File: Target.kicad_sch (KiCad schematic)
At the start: 63 parts, among them J10 PWR Header, J11 LP Extension Heder, J12 LP Header right, J13 PWR Header, J8 Jumper, J9 LP Header left, SW2 RESET, SW3 BOOT, U10 WS2812B-2020, U11 WS2812B-2020, U12 WS2812B-2020, U13 WS2812B-2020, U14 WS2812B-2020, U15 WS2812B-2020, U16 WS2812B-2020, U6 25Q64, U7 APS6404L-3SQR, U8 RP2350_80QFN, U9 WS2812B-2020, Y2 12MHz

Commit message: Renamed files.
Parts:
- J8: symbol rp2040-launchpad-PCB:Jumper -> rp2350b-launchpad-PCB:Jumper
- U10, U11, U12, U13, U14, U15, U16, U9: symbol rp2040-launchpad-PCB:WS2812B-2020 -> rp2350b-launchpad-PCB:WS2812B-2020
- U6: symbol rp2040-launchpad-PCB:25Q32 -> rp2350b-launchpad-PCB:25Q32
- U7: symbol rp2040-launchpad-PCB:APS6404L-3SQR -> rp2350b-launchpad-PCB:APS6404L-3SQR
- U8: symbol rp2040-launchpad-PCB:RP2350_80QFN -> rp2350b-launchpad-PCB:RP2350_80QFN
- USB2: symbol rp2040-launchpad-PCB:USB-C-Socket -> rp2350b-launchpad-PCB:USB-C-Socket
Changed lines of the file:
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@@
 	)
 	(symbol
-		(lib_id "rp2040-launchpad-PCB:25Q32")
+		(lib_id "rp2350b-launchpad-PCB:25Q32")
 		(at 46.99 153.67 0)
 		(mirror y)
@@
 	)
 	(symbol
-		(lib_id "rp2040-launchpad-PCB:WS2812B-2020")
+		(lib_id "rp2350b-launchpad-PCB:WS2812B-2020")
 		(at 165.1 139.7 0)
 		(unit 1)
@@
 	)
 	(symbol
-		(lib_id "rp2040-launchpad-PCB:WS2812B-2020")
+		(lib_id "rp2350b-launchpad-PCB:WS2812B-2020")
 		(at 180.34 139.7 0)
 		(unit 1)
@@
 	)
 	(symbol
-		(lib_id "rp2040-launchpad-PCB:WS2812B-2020")
+		(lib_id "rp2350b-launchpad-PCB:WS2812B-2020")
 		(at 195.58 139.7 0)
 		(unit 1)
@@
 	)
 	(symbol
-		(lib_id "rp2040-launchpad-PCB:WS2812B-2020")
+		(lib_id "rp2350b-launchpad-PCB:WS2812B-2020")
 		(at 210.82 139.7 0)
 		(unit 1)
@@
 	)
 	(symbol
-		(lib_id "rp2040-launchpad-PCB:WS2812B-2020")
+		(lib_id "rp2350b-launchpad-PCB:WS2812B-2020")
 		(at 226.06 139.7 0)
 		(unit 1)
@@
 	)
 	(symbol
-		(lib_id "rp2040-launchpad-PCB:WS2812B-2020")
+		(lib_id "rp2350b-launchpad-PCB:WS2812B-2020")
 		(at 241.3 139.7 0)
 		(unit 1)
@@
 	)
 	(symbol
-		(lib_id "rp2040-launchpad-PCB:WS2812B-2020")
+		(lib_id "rp2350b-launchpad-PCB:WS2812B-2020")
 		(at 256.54 139.7 0)
 		(unit 1)
@@
 	)
 	(symbol
-		(lib_id "rp2040-launchpad-PCB:WS2812B-2020")
+		(lib_id "rp2350b-launchpad-PCB:WS2812B-2020")
 		(at 271.78 139.7 0)
 		(unit 1)
@@
 		)
 		(instances
-			(project "rp2040-launchpad-PCB"
+			(project "rp2350b-launchpad-PCB"
 				(path "/60290668-847e-40fe-8544-1cbbc26023b6/00000000-0000-0000-0000-0000626cc112"
 					(reference "#PWR040")
@@
 		)
 		(instances
-			(project "rp2040-launchpad-PCB"
+			(project "rp2350b-launchpad-PCB"
 				(path "/60290668-847e-40fe-8544-1cbbc26023b6/00000000-0000-0000-0000-0000626cc112"
 					(reference "R29")
@@
 		)
 		(instances
-			(project "rp2040-launchpad-PCB"
+			(project "rp2350b-launchpad-PCB"
 				(path "/60290668-847e-40fe-8544-1cbbc26023b6/00000000-0000-0000-0000-0000626cc112"
 					(reference "#PWR046")
@@
 		)
 		(instances
-			(project "rp2040-launchpad-PCB"
+			(project "rp2350b-launchpad-PCB"
 				(path "/60290668-847e-40fe-8544-1cbbc26023b6/00000000-0000-0000-0000-0000626cc112"
 					(reference "R33")
@@
 		)
 		(instances
-			(project "rp2040-launchpad-PCB"
+			(project "rp2350b-launchpad-PCB"
 				(path "/60290668-847e-40fe-8544-1cbbc26023b6/00000000-0000-0000-0000-0000626cc112"
 					(reference "#PWR043")
@@
 		)
 		(instances
-			(project "rp2040-launchpad-PCB"
+			(project "rp2350b-launchpad-PCB"
 				(path "/60290668-847e-40fe-8544-1cbbc26023b6/00000000-0000-0000-0000-0000626cc112"
 					(reference "R32")
@@
 		)
 		(instances
-			(project "rp2040-launchpad-PCB"
+			(project "rp2350b-launchpad-PCB"
 				(path "/60290668-847e-40fe-8544-1cbbc26023b6/00000000-0000-0000-0000-0000626cc112"
 					(reference "R17")
@@
 		)
 		(instances
-			(project "rp2040-launchpad-PCB"
+			(project "rp2350b-launchpad-PCB"
 				(path "/60290668-847e-40fe-8544-1cbbc26023b6/00000000-0000-0000-0000-0000626cc112"
 					(reference "L2")
@@
 		)
 		(instances
-			(project "rp2040-launchpad-PCB"
+			(project "rp2350b-launchpad-PCB"
 				(path "/60290668-847e-40fe-8544-1cbbc26023b6/00000000-0000-0000-0000-0000626cc112"
 					(reference "C24")
@@
 		)
 		(instances
-			(project "rp2040-launchpad-PCB"
+			(project "rp2350b-launchpad-PCB"
 				(path "/60290668-847e-40fe-8544-1cbbc26023b6/00000000-0000-0000-0000-0000626cc112"
 					(reference "#PWR034")
@@
 		)
 		(instances
-			(project "rp2040-launchpad-PCB"
+			(project "rp2350b-launchpad-PCB"
 				(path "/60290668-847e-40fe-8544-1cbbc26023b6/00000000-0000-0000-0000-0000626cc112"
 					(reference "C26")
@@
 		)
 		(instances
-			(project "rp2040-launchpad-PCB"
+			(project "rp2350b-launchpad-PCB"
 				(path "/60290668-847e-40fe-8544-1cbbc26023b6/00000000-0000-0000-0000-0000626cc112"
 					(reference "#PWR035")
@@
 		)
 		(instances
-			(project "rp2040-launchpad-PCB"
+			(project "rp2350b-launchpad-PCB"
 				(path "/60290668-847e-40fe-8544-1cbbc26023b6/00000000-0000-0000-0000-0000626cc112"
 					(reference "R30")
@@
 		)
 		(instances
-			(project "rp2040-launchpad-PCB"
+			(project "rp2350b-launchpad-PCB"
 				(path "/60290668-847e-40fe-8544-1cbbc26023b6/00000000-0000-0000-0000-0000626cc112"
 					(reference "C29")
@@
 		)
 		(instances
-			(project "rp2040-launchpad-PCB"
+			(project "rp2350b-launchpad-PCB"
 				(path "/60290668-847e-40fe-8544-1cbbc26023b6/00000000-0000-0000-0000-0000626cc112"
 					(reference "#PWR038")
@@
 		)
 		(instances
-			(project "rp2040-launchpad-PCB"
+			(project "rp2350b-launchpad-PCB"
 				(path "/60290668-847e-40fe-8544-1cbbc26023b6/00000000-0000-0000-0000-0000626cc112"
 					(reference "R20")
@@
 		)
 		(instances
-			(project "rp2040-launchpad-PCB"
+			(project "rp2350b-launchpad-PCB"
 				(path "/60290668-847e-40fe-8544-1cbbc26023b6/00000000-0000-0000-0000-0000626cc112"
 					(reference "#PWR026")
@@
 		)
 		(instances
-			(project "rp2040-launchpad-PCB"
+			(project "rp2350b-launchpad-PCB"
 				(path "/60290668-847e-40fe-8544-1cbbc26023b6/00000000-0000-0000-0000-0000626cc112"
 					(reference "C30")
@@
 		)
 		(instances
-			(project "rp2040-launchpad-PCB"
+			(project "rp2350b-launchpad-PCB"
 				(path "/60290668-847e-40fe-8544-1cbbc26023b6/00000000-0000-0000-0000-0000626cc112"
 					(reference "S2")
@@
 		)
 		(instances
-			(project "rp2040-launchpad-PCB"
+			(project "rp2350b-launchpad-PCB"
 				(path "/60290668-847e-40fe-8544-1cbbc26023b6/00000000-0000-0000-0000-0000626cc112"
 					(reference "R18")
@@
 		)
 		(instances
-			(project "rp2040-launchpad-PCB"
+			(project "rp2350b-launchpad-PCB"
 				(path "/60290668-847e-40fe-8544-1cbbc26023b6/00000000-0000-0000-0000-0000626cc112"
 					(reference "#PWR031")
@@
 		)
 		(instances
-			(project "rp2040-launchpad-PCB"
+			(project "rp2350b-launchpad-PCB"
 				(path "/60290668-847e-40fe-8544-1cbbc26023b6/00000000-0000-0000-0000-0000626cc112"
 					(reference "#PWR033")
@@
 		)
 		(instances
-			(project "rp2040-launchpad-PCB"
+			(project "rp2350b-launchpad-PCB"
 				(path "/60290668-847e-40fe-8544-1cbbc26023b6/00000000-0000-0000-0000-0000626cc112"
 					(reference "#PWR030")
@@
 	)
 	(symbol
-		(lib_id "rp2040-launchpad-PCB:RP2350_80QFN")
+		(lib_id "rp2350b-launchpad-PCB:RP2350_80QFN")
 		(at 97.79 99.06 0)
 		(unit 1)
@@
 		)
 		(instances
-			(project "rp2040-launchpad-PCB"
+			(project "rp2350b-launchpad-PCB"
 				(path "/60290668-847e-40fe-8544-1cbbc26023b6/00000000-0000-0000-0000-0000626cc112"
 					(reference "C25")
@@
 		)
 		(instances
-			(project "rp2040-launchpad-PCB"
+			(project "rp2350b-launchpad-PCB"
 				(path "/60290668-847e-40fe-8544-1cbbc26023b6/00000000-0000-0000-0000-0000626cc112"
 					(reference "#PWR041")
@@
 		)
 		(instances
-			(project "rp2040-launchpad-PCB"
+			(project "rp2350b-launchpad-PCB"
 				(path "/60290668-847e-40fe-8544-1cbbc26023b6/00000000-0000-0000-0000-0000626cc112"
 					(reference "C31")
@@
 		)
 		(instances
-			(project "rp2040-launchpad-PCB"
+			(project "rp2350b-launchpad-PCB"
 				(path "/60290668-847e-40fe-8544-1cbbc26023b6/00000000-0000-0000-0000-0000626cc112"
 					(reference "R28")
@@
 	)
 	(symbol
-		(lib_id "rp2040-launchpad-PCB:APS6404L-3SQR")
+		(lib_id "rp2350b-launchpad-PCB:APS6404L-3SQR")
 		(at 48.26 182.88 0)
 		(unit 1)
@@
 		)
 		(instances
-			(project "rp2040-launchpad-PCB"
+			(project "rp2350b-launchpad-PCB"
 				(path "/60290668-847e-40fe-8544-1cbbc26023b6/00000000-0000-0000-0000-0000626cc112"
 					(reference "R26")
@@
 		)
 		(instances
-			(project "rp2040-launchpad-PCB"
+			(project "rp2350b-launchpad-PCB"
 				(path "/60290668-847e-40fe-8544-1cbbc26023b6/00000000-0000-0000-0000-0000626cc112"
 					(reference "#PWR042")
@@
 	)
 	(symbol
-		(lib_id "rp2040-launchpad-PCB:Jumper")
+		(lib_id "rp2350b-launchpad-PCB:Jumper")
 		(at 154.94 130.81 90)
 		(unit 1)
@@
 		)
 		(instances
-			(project "rp2040-launchpad-PCB"
+			(project "rp2350b-launchpad-PCB"
 				(path "/60290668-847e-40fe-8544-1cbbc26023b6/00000000-0000-0000-0000-0000626cc112"
 					(reference "C39")
@@
 	)
 	(symbol
-		(lib_id "rp2040-launchpad-PCB:USB-C-Socket")
+		(lib_id "rp2350b-launchpad-PCB:USB-C-Socket")
 		(at 43.18 115.57 0)
 		(unit 1)
@@
 		)
 		(instances
-			(project "rp2040-launchpad-PCB"
+			(project "rp2350b-launchpad-PCB"
 				(path "/60290668-847e-40fe-8544-1cbbc26023b6/00000000-0000-0000-0000-0000626cc112"
 					(reference "USB2")
@@
 		)
 		(instances
-			(project "rp2040-launchpad-PCB"
+			(project "rp2350b-launchpad-PCB"
 				(path "/60290668-847e-40fe-8544-1cbbc26023b6/00000000-0000-0000-0000-0000626cc112"
 					(reference "C21")
@@
 		)
 		(instances
-			(project "rp2040-launchpad-PCB"
+			(project "rp2350b-launchpad-PCB"
 				(path "/60290668-847e-40fe-8544-1cbbc26023b6/00000000-0000-0000-0000-0000626cc112"
 					(reference "R19")
@@
 		)
 		(instances
-			(project "rp2040-launchpad-PCB"
+			(project "rp2350b-launchpad-PCB"
 				(path "/60290668-847e-40fe-8544-1cbbc26023b6/00000000-0000-0000-0000-0000626cc112"
 					(reference "C23")
@@
 		)
 		(instances
-			(project "rp2040-launchpad-PCB"
+			(project "rp2350b-launchpad-PCB"
 				(path "/60290668-847e-40fe-8544-1cbbc26023b6/00000000-0000-0000-0000-0000626cc112"
 					(reference "C41")
@@
 		)
 		(instances
-			(project "rp2040-launchpad-PCB"
+			(project "rp2350b-launchpad-PCB"
 				(path "/60290668-847e-40fe-8544-1cbbc26023b6/00000000-0000-0000-0000-0000626cc112"
 					(reference "C40")
@@
 		)
 		(instances
-			(project "rp2040-launchpad-PCB"
+			(project "rp2350b-launchpad-PCB"
 				(path "/60290668-847e-40fe-8544-1cbbc26023b6/00000000-0000-0000-0000-0000626cc112"
 					(reference "#PWR036")

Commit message: Fixes to manual renaming...
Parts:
- removed U6: 25Q64, Package_SON:WSON-8-1EP_6x5mm_P1.27mm_EP3.4x4.3mm, symbol rp2350b-launchpad-PCB:25Q32
- added U6: 25Q64, Package_SON:WSON-8-1EP_6x5mm_P1.27mm_EP3.4x4.3mm, symbol rp2350b-launchpad-PCB:25Q64
- S1, S2, SW2: footprint rp2350-launchpad:DIPT-1188E -> rp2350b-launchpad-PCB:DIPT-1188E
- SW3: footprint rp2350-launchpad:KMR2-Switch -> rp2350b-launchpad-PCB:KMR2-Switch
- U10, U11, U12, U13, U14, U15, U16, U9: footprint rp2350-launchpad:WS2812B-2020 -> rp2350b-launchpad-PCB:WS2812B-2020
- USB2: footprint rp2350-launchpad:USB-C-GCT-USB4105 -> rp2350b-launchpad-PCB:USB-C-GCT-USB4105
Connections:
- net +3V3: now also U6.8 (VCC)
- net BOOT: now also U6.1 (~{CS})
- net GND: now also U6.4 (GND), U6.9 (SHLD)
- net SCLK: now also U6.6 (CLK)
- net SD0: now also U6.5 (DI(IO0))
- net SD1: now also U6.2 (DO(IO1))
- net SD2: now also U6.3 (~{WP}(IO2))
- net SD3: now also U6.7 (~{HOLD}(IO3))
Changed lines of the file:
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@@
 	)
 	(junction
-		(at 33.02 157.48)
-		(diameter 0)
-		(color 0 0 0 0)
-	)
-	(junction
 		(at 33.02 176.53)
 		(diameter 0)
@@
 	)
 	(junction
+		(at 33.02 157.48)
+		(diameter 0)
+		(color 0 0 0 0)
+	)
+	(junction
 		(at 49.53 46.99)
 		(diameter 0)
@@
 			)
 		)
-		(property "Footprint" "rp2350-launchpad:DIPT-1188E"
+		(property "Footprint" "rp2350b-launchpad-PCB:DIPT-1188E"
 			(at 115.57 186.69 0)
 			(effects
@@
 			)
 		)
-		(property "Footprint" "rp2350-launchpad:KMR2-Switch"
+		(property "Footprint" "rp2350b-launchpad-PCB:KMR2-Switch"
 			(at 137.16 186.69 0)
 			(effects
@@
 	)
 	(symbol
-		(lib_id "rp2350b-launchpad-PCB:25Q32")
-		(at 46.99 153.67 0)
-		(mirror y)
-		(unit 1)
-		(exclude_from_sim no)
-		(in_bom yes)
-		(on_board yes)
-		(dnp no)
-		(property "Reference" "U6"
-			(at 39.37 143.51 0)
-			(effects
-				(font
-					(size 1.27 1.27)
-				)
-			)
-		)
-		(property "Value" "25Q64"
-			(at 47.625 163.83 0)
-			(effects
-				(font
-					(size 1.27 1.27)
-				)
-			)
-		)
-		(property "Footprint" "Package_SON:WSON-8-1EP_6x5mm_P1.27mm_EP3.4x4.3mm"
-			(at 44.45 153.67 0)
-			(effects
-				(font
-					(size 1.524 1.524)
-				)
-				(hide yes)
-			)
-		)
-		(property "Datasheet" "https://www.digikey.de/de/products/detail/winbond-electronics/W25Q32JWZPIQ/8568189"
-			(at 44.45 153.67 0)
-			(effects
-				(font
-					(size 1.524 1.524)
-				)
-				(hide yes)
-			)
-		)
-		(property "Description" ""
-			(at 46.99 153.67 0)
-			(effects
-				(font
-					(size 1.27 1.27)
-				)
-				(hide yes)
-			)
-		)
-		(pin "1"
-		)
-		(pin "2"
-		)
-		(pin "3"
-		)
-		(pin "4"
-		)
-		(pin "5"
-		)
-		(pin "6"
-		)
-		(pin "7"
-		)
-		(pin "8"
-		)
-		(pin "9"
-		)
-		(instances
-			(project ""
-				(path "/60290668-847e-40fe-8544-1cbbc26023b6/00000000-0000-0000-0000-0000626cc112"
-					(reference "U6")
-					(unit 1)
-				)
-			)
-		)
-	)
-	(symbol
 		(lib_id "Device:R")
 		(at 58.42 86.36 90)
@@
 			)
 		)
-		(property "Footprint" "rp2350-launchpad:WS2812B-2020"
+		(property "Footprint" "rp2350b-launchpad-PCB:WS2812B-2020"
 			(at 165.1 139.7 0)
 			(effects
@@
 			)
 		)
-		(property "Footprint" "rp2350-launchpad:WS2812B-2020"
+		(property "Footprint" "rp2350b-launchpad-PCB:WS2812B-2020"
 			(at 180.34 139.7 0)
 			(effects
@@
 			)
 		)
-		(property "Footprint" "rp2350-launchpad:WS2812B-2020"
+		(property "Footprint" "rp2350b-launchpad-PCB:WS2812B-2020"
 			(at 195.58 139.7 0)
 			(effects
@@
 			)
 		)
-		(property "Footprint" "rp2350-launchpad:WS2812B-2020"
+		(property "Footprint" "rp2350b-launchpad-PCB:WS2812B-2020"
 			(at 210.82 139.7 0)
 			(effects
@@
 			)
 		)
-		(property "Footprint" "rp2350-launchpad:WS2812B-2020"
+		(property "Footprint" "rp2350b-launchpad-PCB:WS2812B-2020"
 			(at 226.06 139.7 0)
 			(effects
@@
 			)
 		)
-		(property "Footprint" "rp2350-launchpad:WS2812B-2020"
+		(property "Footprint" "rp2350b-launchpad-PCB:WS2812B-2020"
 			(at 241.3 139.7 0)
 			(effects
@@
 			)
 		)
-		(property "Footprint" "rp2350-launchpad:WS2812B-2020"
+		(property "Footprint" "rp2350b-launchpad-PCB:WS2812B-2020"
 			(at 256.54 139.7 0)
 			(effects
@@
 			)
 		)
-		(property "Footprint" "rp2350-launchpad:WS2812B-2020"
+		(property "Footprint" "rp2350b-launchpad-PCB:WS2812B-2020"
 			(at 271.78 139.7 0)
 			(effects
@@
 			)
 		)
-		(property "Footprint" "rp2350-launchpad:DIPT-1188E"
+		(property "Footprint" "rp2350b-launchpad-PCB:DIPT-1188E"
 			(at 175.26 116.84 0)
 			(effects
@@
 	)
 	(symbol
+		(lib_id "rp2350b-launchpad-PCB:25Q64")
+		(at 46.99 153.67 0)
+		(mirror y)
+		(unit 1)
+		(exclude_from_sim no)
+		(in_bom yes)
+		(on_board yes)
+		(dnp no)
+		(property "Reference" "U6"
+			(at 39.37 143.51 0)
+			(effects
+				(font
+					(size 1.27 1.27)
+				)
+			)
+		)
+		(property "Value" "25Q64"
+			(at 41.91 163.83 0)
+			(effects
+				(font
+					(size 1.27 1.27)
+				)
+			)
+		)
+		(property "Footprint" "Package_SON:WSON-8-1EP_6x5mm_P1.27mm_EP3.4x4.3mm"
+			(at 44.45 140.716 0)
+			(effects
+				(font
+					(size 1.524 1.524)
+				)
+				(hide yes)
+			)
+		)
+		(property "Datasheet" "https://www.digikey.de/de/products/detail/winbond-electronics/W25Q64JWZPIQ/11584719"
+			(at 42.672 167.132 0)
+			(effects
+				(font
+					(size 1.524 1.524)
+				)
+				(hide yes)
+			)
+		)
+		(property "Description" ""
+			(at 46.99 153.67 0)
+			(effects
+				(font
+					(size 1.27 1.27)
+				)
+				(hide yes)
+			)
+		)
+		(pin "7"
+		)
+		(pin "1"
+		)
+		(pin "8"
+		)
+		(pin "9"
+		)
+		(pin "6"
+		)
+		(pin "5"
+		)
+		(pin "2"
+		)
+		(pin "4"
+		)
+		(pin "3"
+		)
+		(instances
+			(project ""
+				(path "/60290668-847e-40fe-8544-1cbbc26023b6/00000000-0000-0000-0000-0000626cc112"
+					(reference "U6")
+					(unit 1)
+				)
+			)
+		)
+	)
+	(symbol
 		(lib_id "Device:R")
 		(at 49.53 50.8 180)
@@
 			)
 		)
-		(property "Footprint" "rp2350-launchpad:DIPT-1188E"
+		(property "Footprint" "rp2350b-launchpad-PCB:DIPT-1188E"
 			(at 175.26 109.22 0)
 			(effects
@@
 			)
 		)
-		(property "Footprint" "rp2350-launchpad:USB-C-GCT-USB4105"
+		(property "Footprint" "rp2350b-launchpad-PCB:USB-C-GCT-USB4105"
 			(at 45.72 106.68 0)
 			(effects

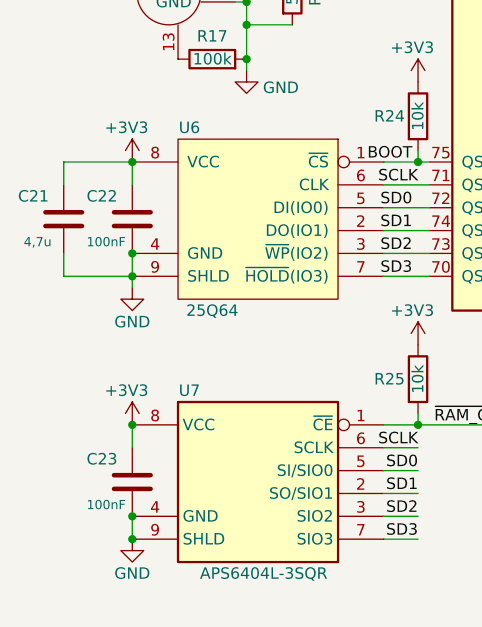
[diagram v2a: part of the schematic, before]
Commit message: Fixed gerber file names.
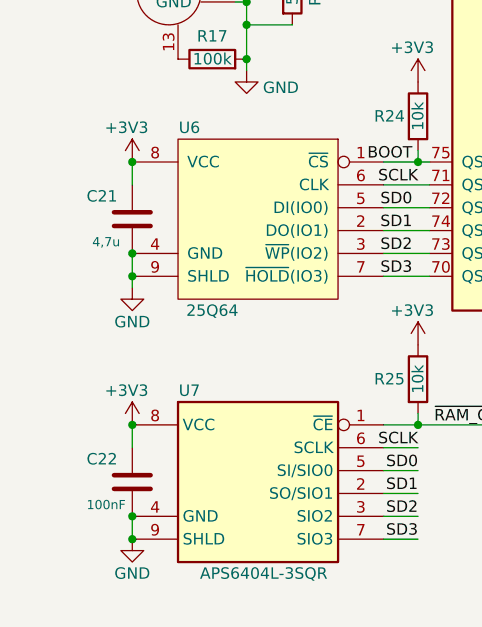
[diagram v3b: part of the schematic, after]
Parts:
- removed C23: 100nF, Capacitor_SMD:C_0402_1005Metric, symbol Device:C
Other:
- moved on the sheet: C21, C22
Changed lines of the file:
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@@
 	)
 	(junction
-		(at 33.02 186.69)
-		(diameter 0)
-		(color 0 0 0 0)
-	)
-	(junction
 		(at 53.34 114.3)
 		(diameter 0)
@@
 	)
 	(junction
+		(at 33.02 186.69)
+		(diameter 0)
+		(color 0 0 0 0)
+	)
+	(junction
 		(at 210.82 129.54)
 		(diameter 0)
@@
 	(wire
 		(pts
-			(xy 25.4 160.02) (xy 33.02 160.02)
-		)
-		(stroke
-			(width 0)
-			(type default)
-		)
-	)
-	(wire
-		(pts
 			(xy 219.71 40.64) (xy 228.6 40.64)
 		)
@@
 	(wire
 		(pts
-			(xy 25.4 157.48) (xy 25.4 160.02)
-		)
-		(stroke
-			(width 0)
-			(type default)
-		)
-	)
-	(wire
-		(pts
 			(xy 195.58 40.64) (xy 207.01 40.64)
 		)
@@
 	(wire
 		(pts
-			(xy 25.4 147.32) (xy 33.02 147.32)
-		)
-		(stroke
-			(width 0)
-			(type default)
-		)
-	)
-	(wire
-		(pts
 			(xy 182.88 109.22) (xy 182.88 116.84)
 		)
@@
 	(wire
 		(pts
-			(xy 25.4 149.86) (xy 25.4 147.32)
-		)
-		(stroke
-			(width 0)
-			(type default)
-		)
-	)
-	(wire
-		(pts
 			(xy 138.43 106.68) (xy 140.97 106.68)
 		)
@@
 	(symbol
 		(lib_id "Device:C")
-		(at 33.02 153.67 0)
+		(at 33.02 182.88 0)
 		(unit 1)
 		(exclude_from_sim no)
@@
 		(dnp no)
 		(property "Reference" "C22"
-			(at 27.94 151.13 0)
+			(at 27.94 180.34 0)
 			(effects
 				(font
@@
 		)
 		(property "Value" "100nF"
-			(at 27.94 156.21 0)
+			(at 27.94 185.42 0)
 			(effects
 				(font
@@
 		)
 		(property "Footprint" "Capacitor_SMD:C_0402_1005Metric"
-			(at 33.02 153.67 0)
+			(at 33.02 182.88 0)
 			(effects
 				(font
@@
 		)
 		(property "Datasheet" "https://www.digikey.de/de/products/detail/kemet/C0603C104J4RAC7013/8572406"
-			(at 33.02 153.67 0)
+			(at 33.02 182.88 0)
 			(effects
 				(font
@@
 		)
 		(property "Description" ""
-			(at 33.02 153.67 0)
+			(at 33.02 182.88 0)
 			(effects
 				(font
@@
 		)
 		(property "MANUFACTURER" "z.B. Kemet"
-			(at 33.02 153.67 0)
+			(at 33.02 182.88 0)
 			(effects
 				(font
@@
 		)
 		(property "STANDARD" "unkritisch"
-			(at 33.02 153.67 0)
+			(at 33.02 182.88 0)
 			(effects
 				(font
@@
 	(symbol
 		(lib_id "Device:C")
-		(at 25.4 153.67 0)
+		(at 33.02 153.67 0)
 		(unit 1)
 		(exclude_from_sim no)
@@
 		(dnp no)
 		(property "Reference" "C21"
-			(at 20.32 151.13 0)
+			(at 27.94 151.13 0)
 			(effects
 				(font
@@
 		)
 		(property "Value" "4,7u"
-			(at 20.955 156.21 0)
+			(at 28.575 156.21 0)
 			(effects
 				(font
@@
 		)
 		(property "Footprint" "Capacitor_SMD:C_0402_1005Metric"
-			(at 25.4 153.67 0)
+			(at 33.02 153.67 0)
 			(effects
 				(font
@@
 		)
 		(property "Datasheet" "https://www.digikey.de/de/products/detail/kemet/C0603C104J4RAC7013/8572406"
-			(at 25.4 153.67 0)
+			(at 33.02 153.67 0)
 			(effects
 				(font
@@
 		)
 		(property "Description" ""
-			(at 25.4 153.67 0)
+			(at 33.02 153.67 0)
 			(effects
 				(font
@@
 		)
 		(property "MANUFACTURER" "z.B. Kemet"
-			(at 25.4 153.67 0)
+			(at 33.02 153.67 0)
 			(effects
 				(font
@@
 		)
 		(property "STANDARD" "unkritisch"
-			(at 25.4 153.67 0)
+			(at 33.02 153.67 0)
 			(effects
 				(font
@@
 					(unit 1)
 				)
-			)
-		)
-	)
-	(symbol
-		(lib_id "Device:C")
-		(at 33.02 182.88 0)
-		(unit 1)
-		(exclude_from_sim no)
-		(in_bom yes)
-		(on_board yes)
-		(dnp no)
-		(property "Reference" "C23"
-			(at 27.94 180.34 0)
-			(effects
-				(font
-					(size 1.27 1.27)
-				)
-				(justify left)
-			)
-		)
-		(property "Value" "100nF"
-			(at 27.94 185.42 0)
-			(effects
-				(font
-					(size 1.016 1.016)
-				)
-				(justify left)
-			)
-		)
-		(property "Footprint" "Capacitor_SMD:C_0402_1005Metric"
-			(at 33.02 182.88 0)
-			(effects
-				(font
-					(size 1.27 1.27)
-				)
-				(hide yes)
-			)
-		)
-		(property "Datasheet" "https://www.digikey.de/de/products/detail/kemet/C0603C104J4RAC7013/8572406"
-			(at 33.02 182.88 0)
-			(effects
-				(font
-					(size 1.27 1.27)
-				)
-				(hide yes)
-			)
-		)
-		(property "Description" ""
-			(at 33.02 182.88 0)
-			(effects
-				(font
-					(size 1.27 1.27)
-				)
-				(hide yes)
-			)
-		)
-		(property "MANUFACTURER" "z.B. Kemet"
-			(at 33.02 182.88 0)
-			(effects
-				(font
-					(size 1.27 1.27)
-				)
-				(hide yes)
-			)
-		)
-		(property "STANDARD" "unkritisch"
-			(at 33.02 182.88 0)
-			(effects
-				(font
-					(size 1.27 1.27)
-				)
-				(hide yes)
-			)
-		)
-		(pin "1"
-		)
-		(pin "2"
-		)
-		(instances
-			(project "rp2350b-launchpad-PCB"
-				(path "/60290668-847e-40fe-8544-1cbbc26023b6/00000000-0000-0000-0000-0000626cc112"
-					(reference "C23")
-					(unit 1)
-				)
